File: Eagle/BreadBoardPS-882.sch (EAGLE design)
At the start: 6 parts

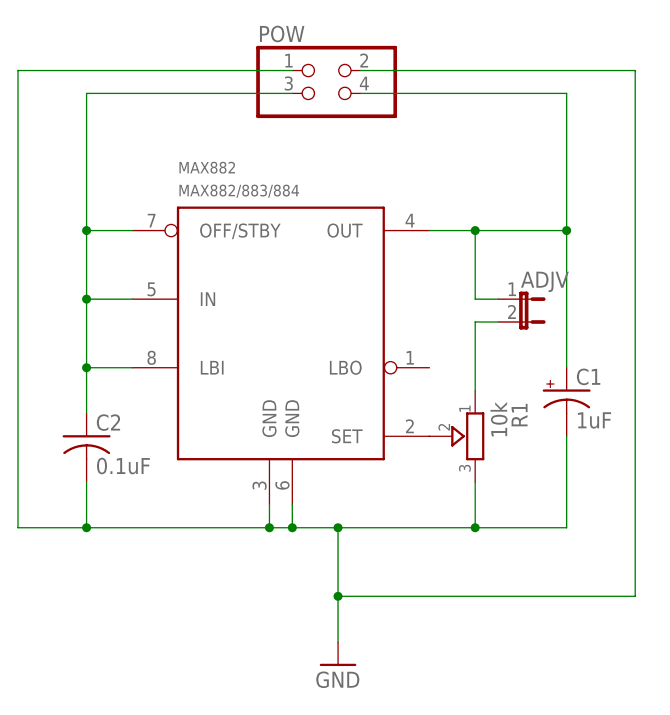
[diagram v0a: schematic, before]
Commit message: Fixed C1 on schematic (and updated the board), README notes.
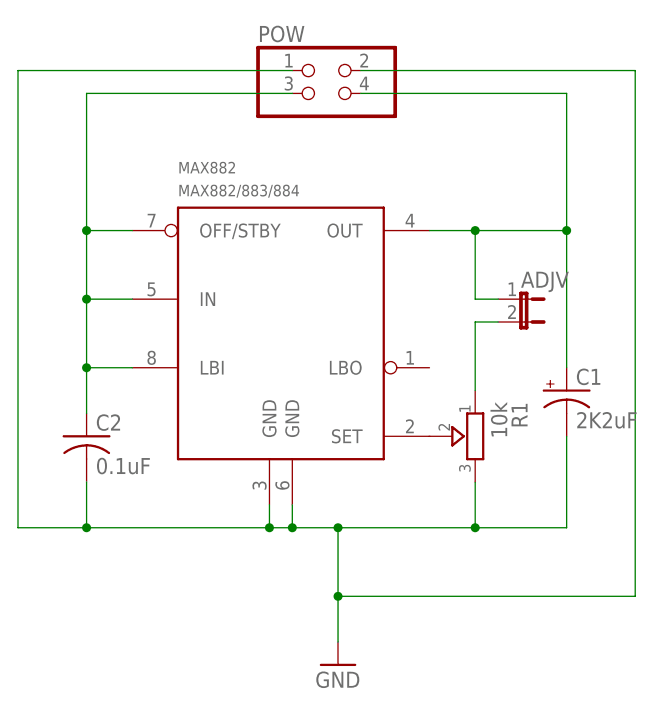
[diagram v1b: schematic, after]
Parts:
- C1: value 1uF -> 2K2uF
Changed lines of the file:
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@@
 <part name="R1" library="dp_devices" deviceset="TRIMMER" device="-3306F" value="10k"/>
 <part name="ADJV" library="jumper" deviceset="JP1E" device=""/>
-<part name="C1" library="rcl" deviceset="CPOL-US" device="E2.5-5" value="1uF"/>
+<part name="C1" library="rcl" deviceset="CPOL-US" device="E2.5-5" value="2K2uF"/>
 <part name="C2" library="resistor" deviceset="C-US" device="025-024X044" value="0.1uF"/>
 <part name="GND1" library="supply1" deviceset="GND" device=""/>

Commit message: Fixed the schematic again because I didn't fix it correctly the first time. My bad.
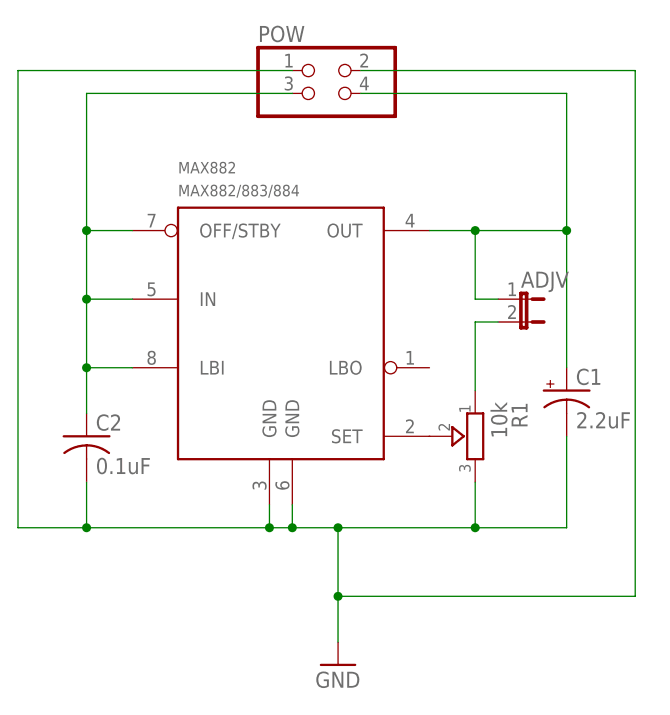
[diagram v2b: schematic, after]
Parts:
- C1: value 2K2uF -> 2.2uF
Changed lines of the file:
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@@
 <?xml version="1.0" encoding="utf-8"?>
 <!DOCTYPE eagle SYSTEM "eagle.dtd">
-<eagle version="7.1.0">
+<eagle version="7.2.0">
 <drawing>
 <settings>
@@
 <part name="R1" library="dp_devices" deviceset="TRIMMER" device="-3306F" value="10k"/>
 <part name="ADJV" library="jumper" deviceset="JP1E" device=""/>
-<part name="C1" library="rcl" deviceset="CPOL-US" device="E2.5-5" value="2K2uF"/>
+<part name="C1" library="rcl" deviceset="CPOL-US" device="E2.5-5" value="2.2uF"/>
 <part name="C2" library="resistor" deviceset="C-US" device="025-024X044" value="0.1uF"/>
 <part name="GND1" library="supply1" deviceset="GND" device=""/>
